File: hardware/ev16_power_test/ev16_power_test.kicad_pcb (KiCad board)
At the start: 4 copper layers, 125 x 80 mm, 185 parts, among them CN1 Conn_05x02_Female, CN2 PJ-242, J1 USB_C_Receptacle, J10 Conn_01x03_Pin, J11 Conn_02x05_Counter_Clockwise, J12 Conn_01x01, J13 Conn_01x01, J14 Conn_01x01, J15 Conn_01x01, J16 Conn_01x01, J17 Conn_01x01, J18 Conn_01x01, J19 Conn_01x01, J2 Conn_01x02_Socket, J20 Conn_01x01, J21 Conn_01x01, J3 AudioJack4, J4 Conn_02x03_Odd_Even, J5 Conn_02x03_Odd_Even, J6 Conn_02x05_Counter_Clockwise, J7 Conn_02x05_Counter_Clockwise, J8 Conn_02x05_Counter_Clockwise, J9 Conn_02x05_Counter_Clockwise, Q1 2N7002, Q2 2N7002, Q3 2N7002, SW1 SW_SPDT, SW2 SW_Push, SW3 SW_Push, SW4 SW_Push, SW5 SW_Push, SW6 SW_Push, SW7 SW_Push, U1 BQ21040DBV, U10 STM32F405RGTx, U12 XC6227C301MR-G, U2 USBLC6-2P6, U3 STM32F072CBTx, U4 CH340C, U5 TPS63060, U6 WM8960CGEFL/RV, U7 ESP32-S3-WROOM-1, U8 M24C02-RMN6TP, U9 TPS2116DRL, Y1 Crystal_GND24

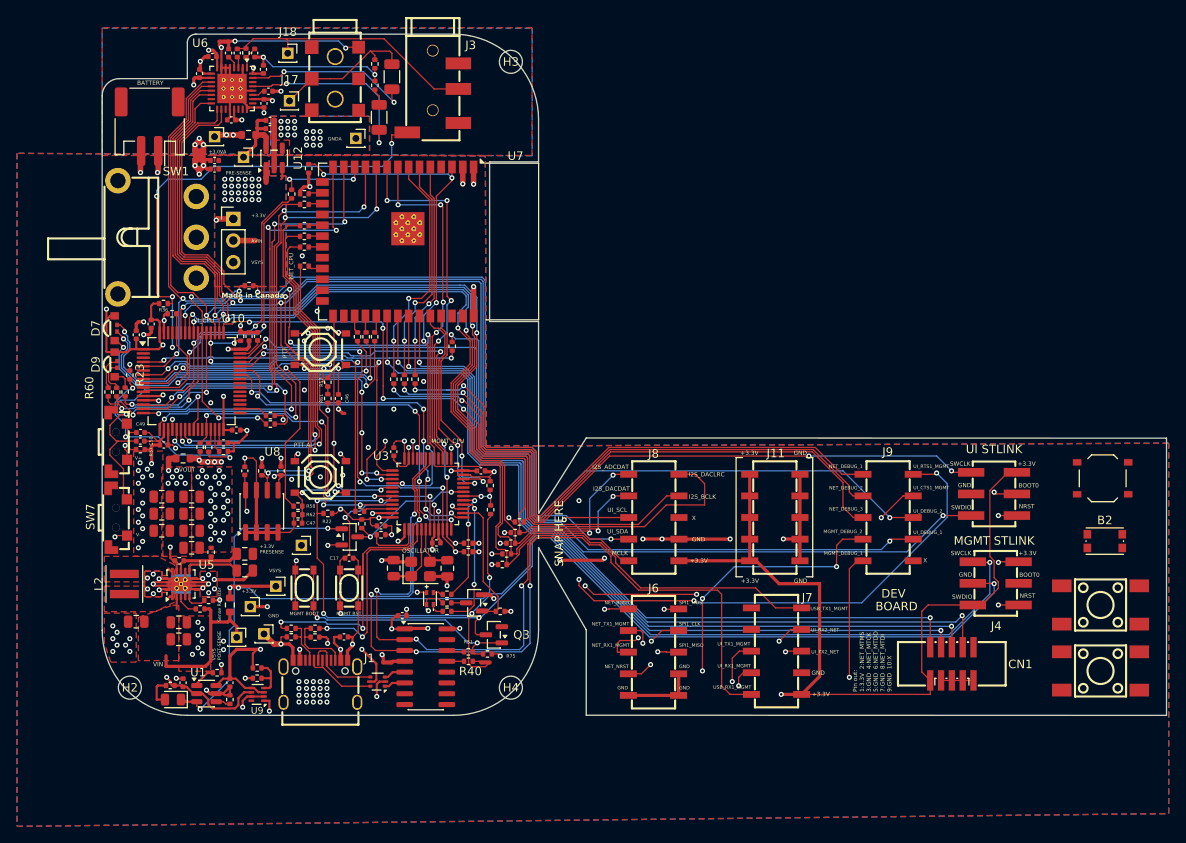
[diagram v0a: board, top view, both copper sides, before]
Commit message: Fixed rotation, added a production file for no tht parts
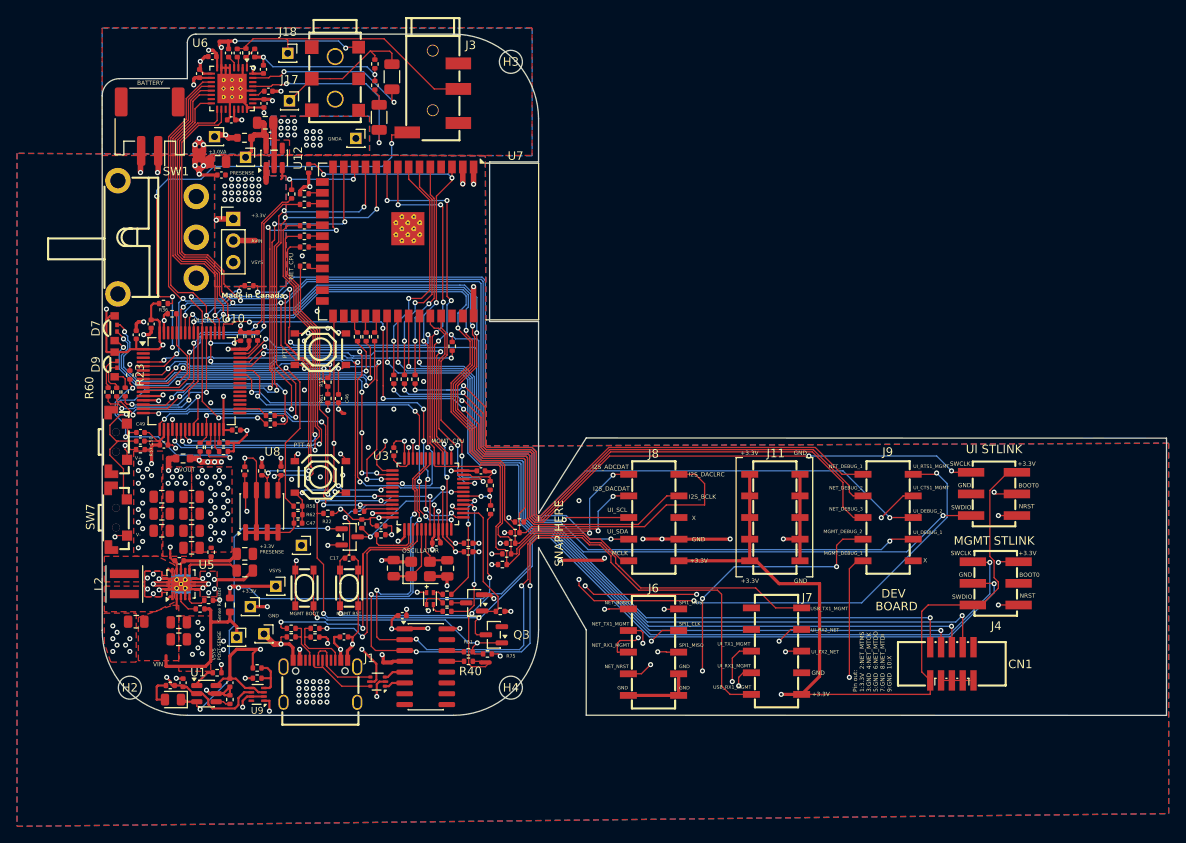
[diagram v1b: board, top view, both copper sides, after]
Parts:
- removed B1: SW_Push_1P1T_XKB_TS-1187A, Button_Switch_SMD:SW_Push_1P1T_XKB_TS-1187A
- removed B2: SW_Push_1P1T_NO_CK_KMR2, Button_Switch_SMD:SW_Push_1P1T_NO_CK_KMR2
- removed B3, B4: SW-SMD_4P-L6.0-W6.0-P4.50-LS9.0_H5.0, Hactar_Footprints:SW-SMD_4P-L6.0-W6.0-P4.5
- removed C51: 100n, Capacitor_SMD:C_0402_1005Metric
- added C11: 100n, Capacitor_SMD:C_0805_2012Metric, F.Cu at (63.6, 45.0)
- C10: footprint Capacitor_SMD:C_0402_1005Metric -> Capacitor_SMD:C_0805_2012Metric
- moved C18 1.76 mm to (69.7, 41.9)
- moved C7 1.06 mm to (64.0, 46.5)
- moved C10 0.89 mm to (69.2, 40.4)
- moved R52 0.59 mm to (66.7, 42.2)
- moved J20 0.24 mm to (66.8, 44.5)
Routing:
- net GND: track 297.7 -> 301.0 mm
- net Net-(J20-Pin_1): track 9.63 -> 8.82 mm
- net +3.0VA: track 22.5 -> 23.0 mm, vias 5 -> 4
- net /AVIN: vias 24 -> 23
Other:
- board text added: "PRESENSE"
- board text removed: "PRE-SENSE"

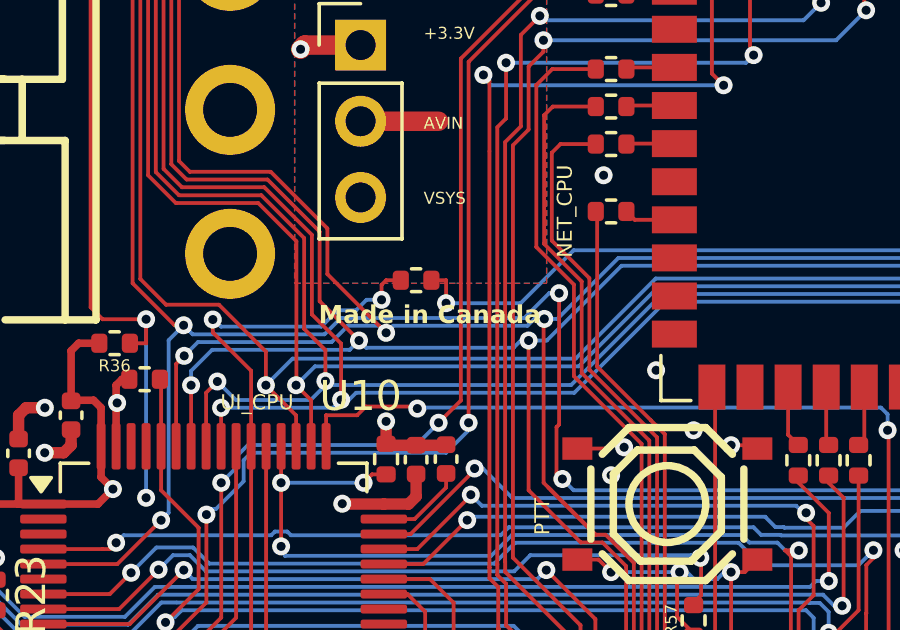
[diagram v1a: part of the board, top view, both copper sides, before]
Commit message: replaced 'made in canada to designed in canada'
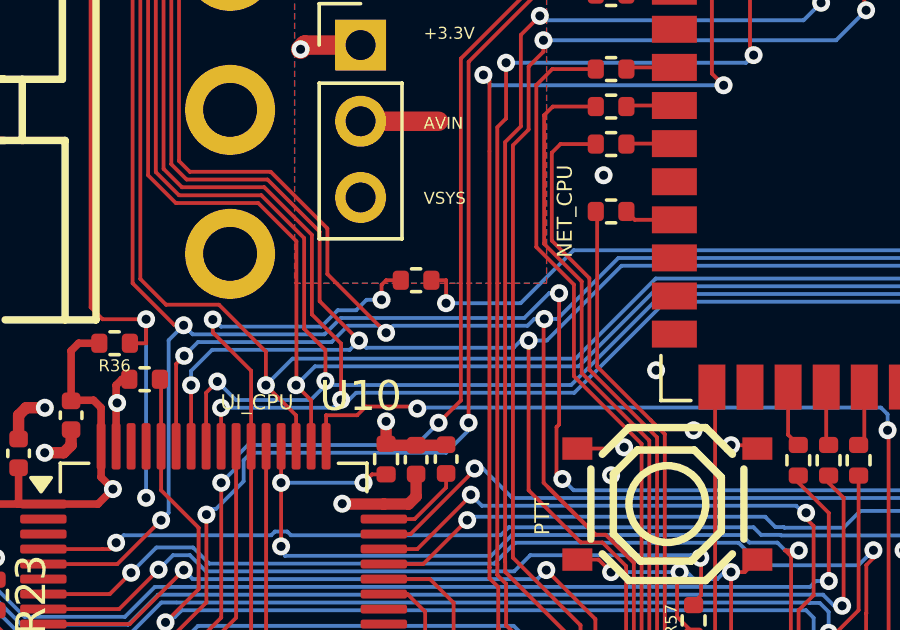
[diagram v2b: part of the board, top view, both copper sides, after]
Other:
- board text added: "Designed in Canada"
- board text removed: "Made in Canada"
